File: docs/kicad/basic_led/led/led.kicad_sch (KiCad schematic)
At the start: 4 parts

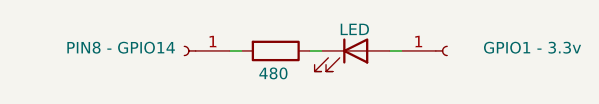
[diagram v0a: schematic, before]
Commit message: Added config cargo
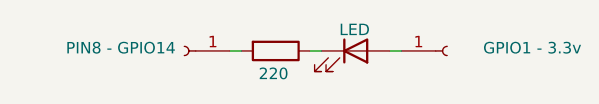
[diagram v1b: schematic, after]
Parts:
- R?: value 480 -> 220
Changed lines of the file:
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@@
       (effects (font (size 1.27 1.27)) (justify left) hide)
     )
-    (property "Value" "480" (id 1) (at 139.065 71.755 90)
+    (property "Value" "220" (id 1) (at 139.065 71.755 90)
       (effects (font (size 1.27 1.27)) (justify left))
     )
@@
     )
     (path "/8c9385ae-02fd-4f31-94a6-2d050942f6fb"
-      (reference "R?") (unit 1) (value "480") (footprint "")
+      (reference "R?") (unit 1) (value "220") (footprint "")
     )
   )
